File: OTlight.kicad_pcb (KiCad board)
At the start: 2 copper layers, 62 parts, among them P1 CONN_01X01, Q1 TEMT6000, Q2 Q_NMOS_GSD, T1 TRANSFO, U1 LM3478, U10 IN-14, U11 IN-14, U12 MAX6931, U13 IN-14, U14 MAX6920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

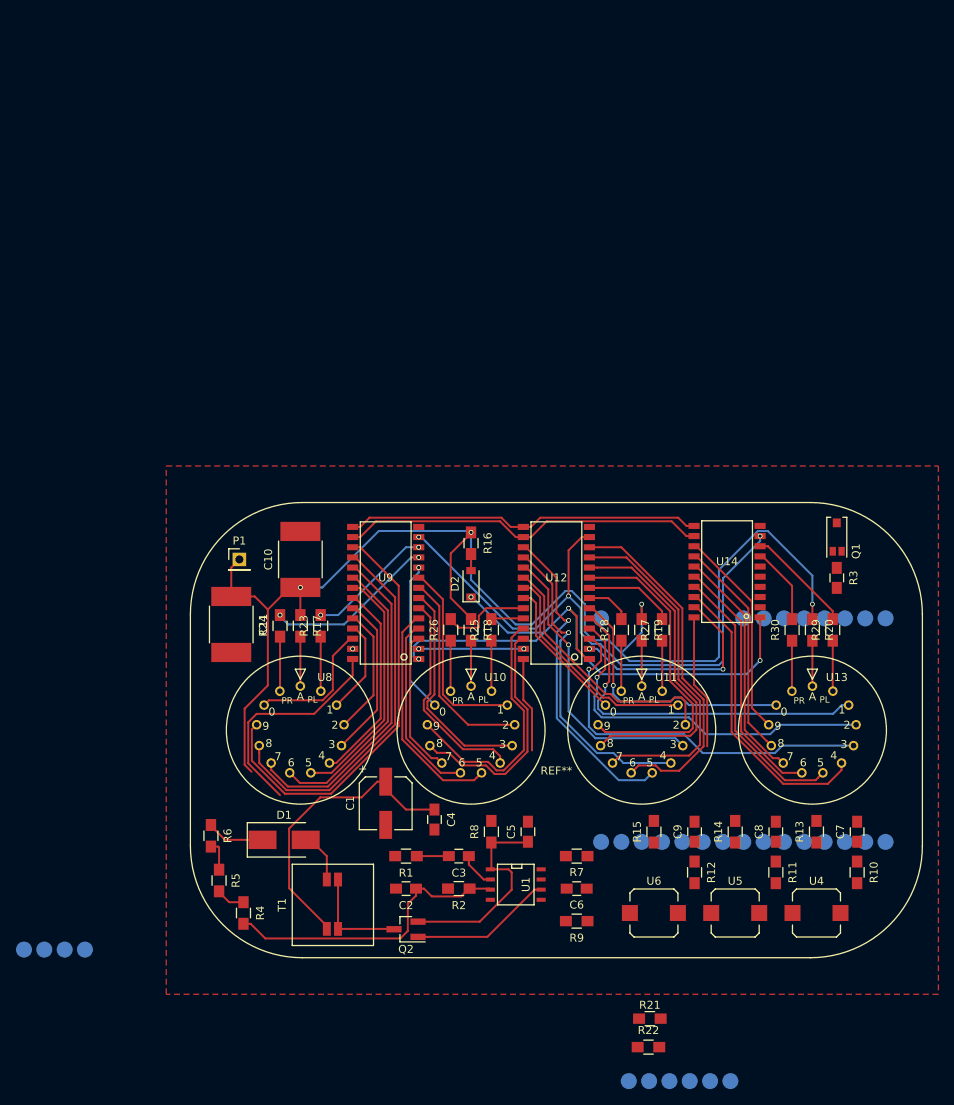
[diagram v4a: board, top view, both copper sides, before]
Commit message: Finished routing PCB
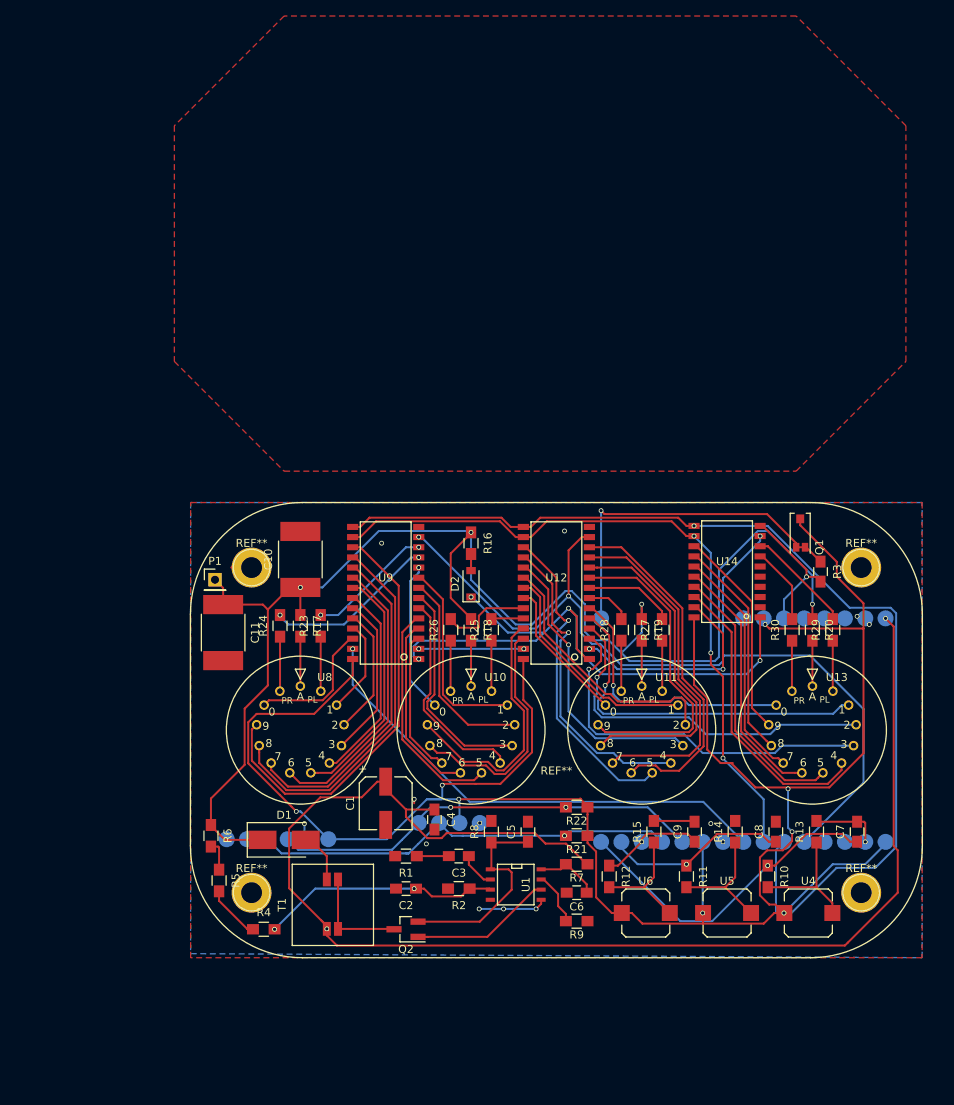
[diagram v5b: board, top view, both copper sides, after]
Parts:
- added REF**: Altoid, BamboulabFootprints:Altoid, B.Cu at (89.4, 104.1)
- added REF**: 1pin, Connectors:1pin, F.Cu at (127.5, 83.8)
- added REF**: 1pin, Connectors:1pin, F.Cu at (51.3, 124.5)
- added REF**: 1pin, Connectors:1pin, F.Cu at (51.3, 83.8)
- added REF**: 1pin, Connectors:1pin, F.Cu at (127.5, 124.5)
- moved U7 65.9 mm to (54.7, 111.4), turned to 90 degrees
- moved U3 51.8 mm to (75.8, 98.3)
- moved R22 31.3 mm to (91.9, 113.8), turned to 180 degrees
- moved R21 24.6 mm to (91.9, 117.3), turned to 180 degrees
- moved R10 11.2 mm to (115.8, 122.4)
- moved R11 11.2 mm to (105.7, 122.4)
- moved R12 10.7 mm to (96.0, 122.4)
- moved Q1 4.60 mm to (119.9, 81.3)
- moved P1 3.97 mm to (46.7, 85.3)
- moved R4 3.25 mm to (52.8, 129.0), turned to 0 degrees
- moved R3 2.18 mm to (122.4, 84.3)
- moved C11 1.44 mm to (47.8, 91.9)
- moved U4 1.02 mm to (120.9, 127.0)
- moved U5 1.02 mm to (110.7, 127.0)
- moved R7 1.02 mm to (91.9, 120.9)
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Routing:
- net +3V3: track 57.0 -> 274.5 mm, vias 0 -> 8
- net +5V: track 37.1 -> 175.1 mm, vias 0 -> 2
- net /CLK: track 44.5 -> 131.8 mm, vias 0 -> 1
- net /DIN: track 0.00 -> 61.5 mm
- net Net-(R22-Pad2): track 0.00 -> 54.2 mm, vias 0 -> 2
- net Net-(R21-Pad2): track 0.00 -> 53.6 mm, vias 0 -> 1
- net GND: track 0.00 -> 46.2 mm, vias 0 -> 14
- net Net-(Q1-Pad2): track 0.00 -> 43.8 mm, vias 0 -> 1
- net /LOAD: track 45.9 -> 87.7 mm, vias 0 -> 3
- net Net-(C7-Pad1): track 0.00 -> 41.0 mm, vias 0 -> 1
- net /BLANK: track 76.6 -> 116.7 mm
- net Net-(C8-Pad1): track 0.00 -> 23.2 mm, vias 0 -> 1
- net Net-(R10-Pad2): track 0.00 -> 15.7 mm
- net Net-(R11-Pad2): track 0.00 -> 15.5 mm
- net Net-(R12-Pad2): track 0.00 -> 15.0 mm
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- added copper zone on B.Cu, net GND

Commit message: Clean up
We are getting there!
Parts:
- renumbered REF** to ?
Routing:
- net GND: track 46.2 -> 2.76 mm, vias 14 -> 92
- net +5V: track 175.1 -> 132.5 mm, vias 2 -> 1
- net /CLK: track 131.8 -> 90.1 mm, vias 1 -> 3
- net +3V3: track 274.5 -> 254.3 mm, vias 8 -> 3
- net Net-(C7-Pad1): track 41.0 -> 36.0 mm
- net (no net): track 1.44 -> 0.00 mm, vias 1 -> 2
- net /LOAD: track 87.7 -> 89.0 mm
- net Net-(R22-Pad2): track 54.2 -> 54.4 mm, vias 2 -> 1

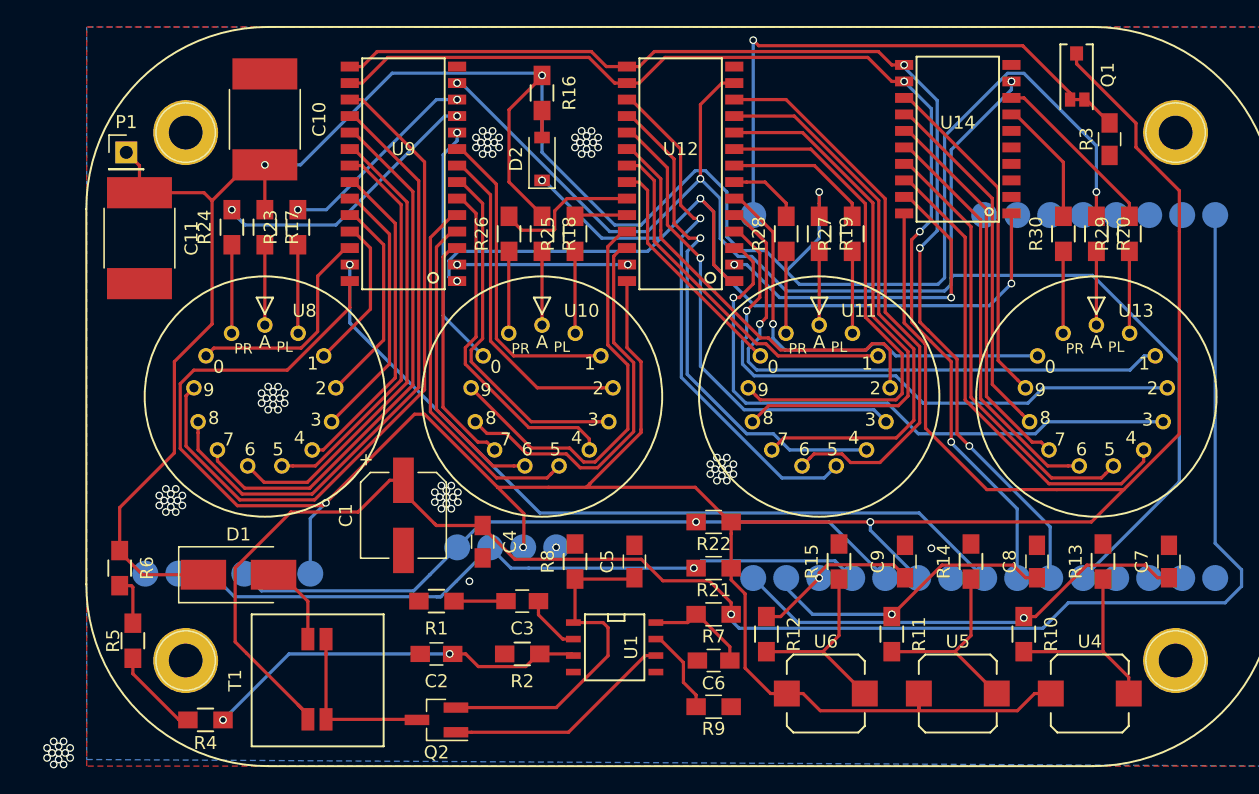
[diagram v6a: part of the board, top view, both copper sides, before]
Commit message: Biribiri silkscreen, clean up, where are the GND vias?
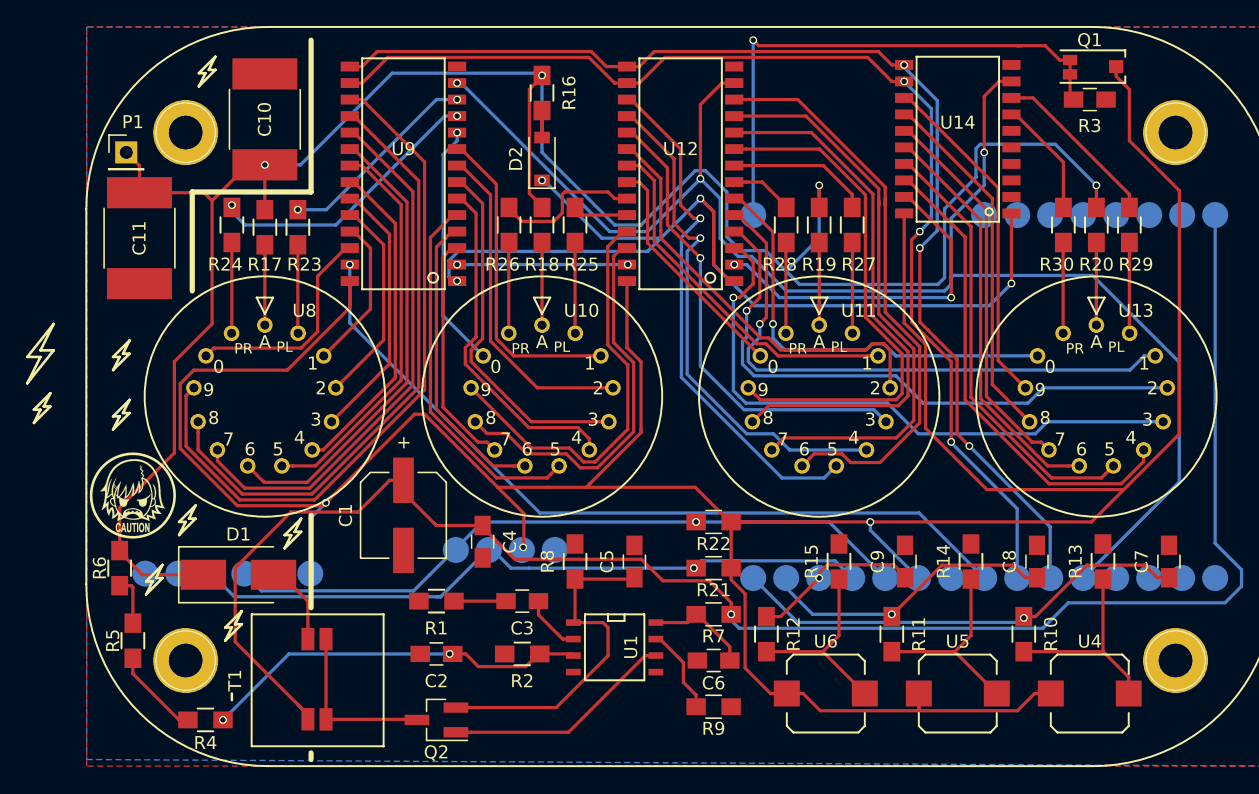
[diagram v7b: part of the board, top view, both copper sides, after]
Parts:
- added G***: LOGO, OTlight:biri2, F.Cu at (47.2, 111.8)
- moved R3 3.41 mm to (120.9, 81.3), turned to 0 degrees
- moved Q1 2.59 mm to (119.4, 78.7), turned to 0 degrees
- moved R18 0.68 mm to (78.7, 90.9)
- moved R19 0.68 mm to (100.1, 90.9)
- moved R20 0.68 mm to (121.4, 90.9)
- moved R25 0.68 mm to (81.3, 90.9)
- moved R26 0.68 mm to (76.2, 90.9)
- moved R27 0.68 mm to (102.6, 90.9)
- moved R28 0.68 mm to (97.5, 90.9)
- moved R29 0.68 mm to (124.0, 90.9)
- moved R30 0.68 mm to (118.9, 90.9)
- moved U3 0.23 mm to (75.7, 98.6)
- moved R24 0.17 mm to (54.9, 90.9)
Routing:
- net /HVout: track 180.7 -> 170.1 mm
- net +3V3: track 254.3 -> 252.0 mm
- net Net-(Q1-Pad2): track 43.8 -> 42.1 mm
- net Net-(U11-Pad8): track 44.1 -> 45.1 mm
- net Net-(U11-Pad9): track 43.7 -> 44.6 mm
- net Net-(R28-Pad2): track 5.67 -> 4.87 mm
- net Net-(R26-Pad1): track 6.31 -> 7.02 mm
- net Net-(R30-Pad2): track 9.68 -> 9.00 mm
- net Net-(R25-Pad1): track 6.31 -> 7.00 mm
- net Net-(R18-Pad2): track 5.68 -> 6.36 mm
- net /BLANK: track 116.7 -> 117.2 mm
- net Net-(R22-Pad2): track 54.4 -> 53.9 mm
- net GND: vias 92 -> 0
- net (no net): vias 2 -> 0

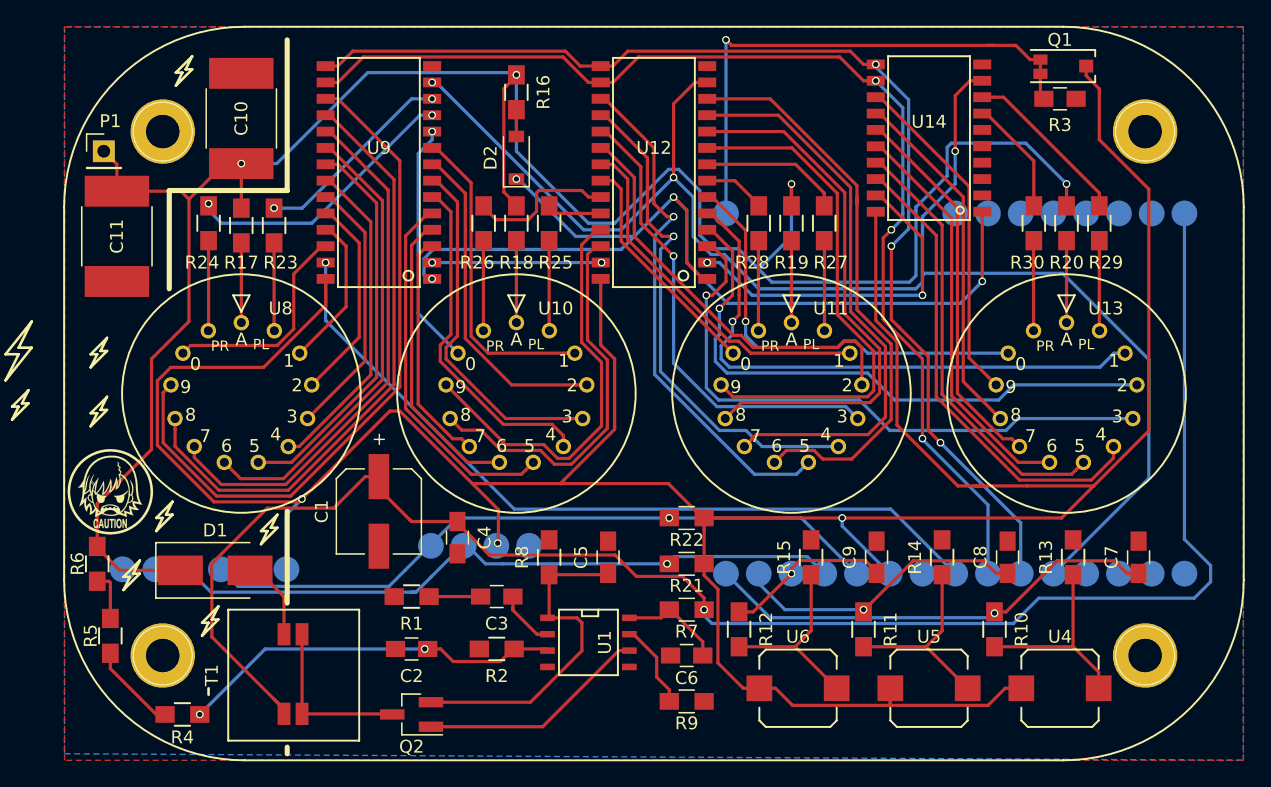
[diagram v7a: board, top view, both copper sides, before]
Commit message: Separated all the pads from the vias... sigh
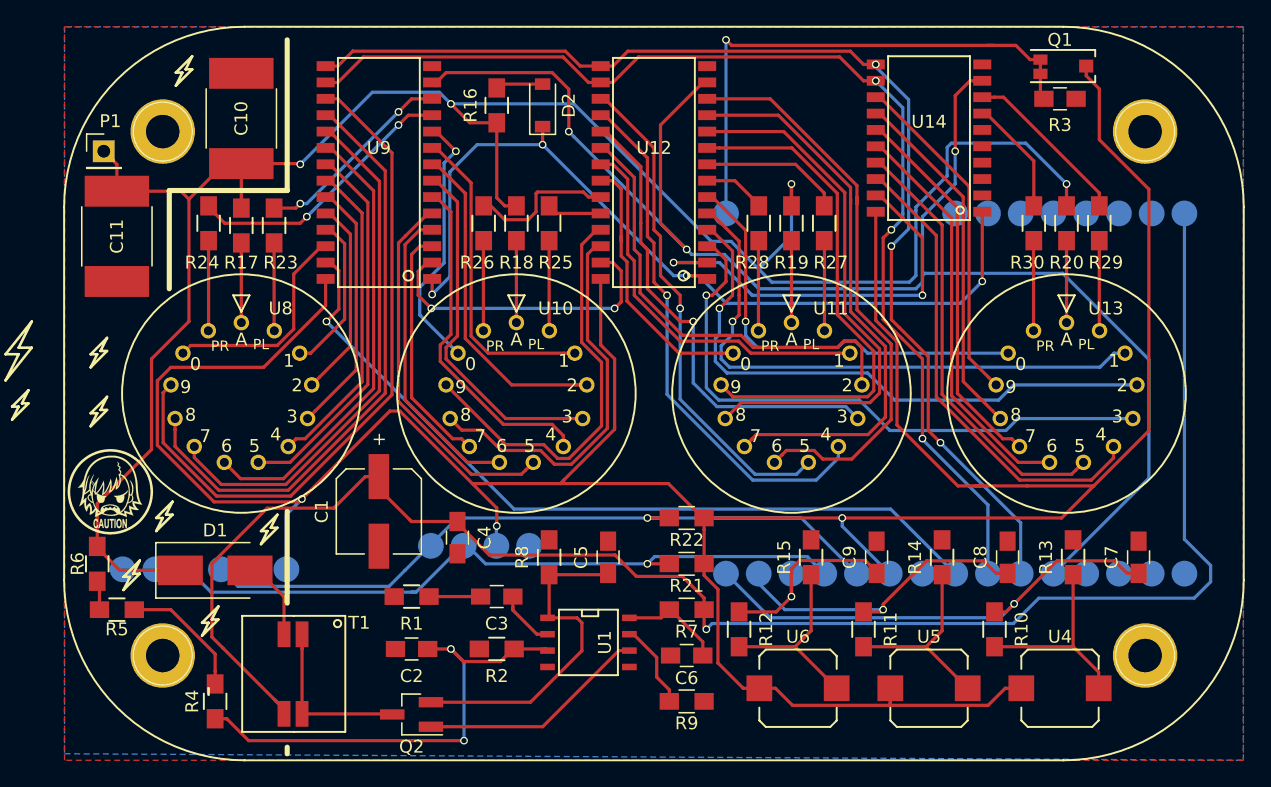
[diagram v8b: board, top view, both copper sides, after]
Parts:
- moved D2 4.54 mm to (80.8, 81.8)
- moved R4 2.74 mm to (55.4, 128.0), turned to 270 degrees
- moved R5 2.09 mm to (47.8, 120.9), turned to 0 degrees
- moved R16 1.83 mm to (77.2, 81.8), turned to 90 degrees
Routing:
- net Net-(U12-Pad27): track 13.1 -> 23.9 mm
- net Net-(D2-Pad1): track 77.8 -> 67.7 mm
- net /HVout: track 170.1 -> 160.8 mm
- net Net-(C2-Pad1): track 29.9 -> 37.7 mm
- net Net-(U12-Pad2): track 27.5 -> 32.7 mm
- net /BLANK: track 117.2 -> 121.5 mm
- net Net-(R4-Pad1): track 6.90 -> 10.0 mm
- net Net-(C9-Pad1): track 13.0 -> 16.1 mm
- net Net-(U11-Pad12): track 18.2 -> 21.0 mm
- net Net-(U11-Pad4): track 32.6 -> 34.9 mm
- net Net-(U11-Pad3): track 28.1 -> 30.4 mm
- net Net-(U11-Pad6): track 39.6 -> 41.6 mm
- net Net-(C7-Pad1): track 36.0 -> 37.7 mm
- net Net-(R22-Pad2): track 53.9 -> 55.6 mm
- net Net-(R21-Pad2): track 53.6 -> 55.3 mm
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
